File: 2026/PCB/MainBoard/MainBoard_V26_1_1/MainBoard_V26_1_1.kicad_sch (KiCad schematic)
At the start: 0 parts

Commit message: 446追加
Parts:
- added U1: STM32F446RETx, Package_QFP:LQFP-64_10x10mm_P0.5mm, symbol MCU_ST_STM32F4:STM32F446RETx
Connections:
- new net: U1.18 (VSS), U1.31 (VSS), U1.47 (VSS), U1.63 (VSS)
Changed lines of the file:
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@@
 	(generator_version "9.0")
 	(paper "A4")
+	(symbol
+		(lib_id "MCU_ST_STM32F4:STM32F446RETx")
+		(at 101.6 92.71 0)
+		(unit 1)
+		(exclude_from_sim no)
+		(in_bom yes)
+		(on_board yes)
+		(dnp no)
+		(fields_autoplaced yes)
+		(property "Reference" "U1"
+			(at 106.2833 138.43 0)
+			(effects
+				(font
+					(size 1.27 1.27)
+				)
+				(justify left)
+			)
+		)
+		(property "Value" "STM32F446RETx"
+			(at 106.2833 140.97 0)
+			(effects
+				(font
+					(size 1.27 1.27)
+				)
+				(justify left)
+			)
+		)
+		(property "Footprint" "Package_QFP:LQFP-64_10x10mm_P0.5mm"
+			(at 83.82 135.89 0)
+			(effects
+				(font
+					(size 1.27 1.27)
+				)
+				(justify right)
+				(hide yes)
+			)
+		)
+		(property "Datasheet" "https://www.st.com/resource/en/datasheet/stm32f446re.pdf"
+			(at 101.6 92.71 0)
+			(effects
+				(font
+					(size 1.27 1.27)
+				)
+				(hide yes)
+			)
+		)
+		(property "Description" "STMicroelectronics Arm Cortex-M4 MCU, 512KB flash, 128KB RAM, 180 MHz, 1.8-3.6V, 50 GPIO, LQFP64"
+			(at 101.6 92.71 0)
+			(effects
+				(font
+					(size 1.27 1.27)
+				)
+				(hide yes)
+			)
+		)
+		(pin "50"
+		)
+		(pin "55"
+		)
+		(pin "57"
+		)
+		(pin "46"
+		)
+		(pin "49"
+		)
+		(pin "34"
+		)
+		(pin "26"
+		)
+		(pin "27"
+		)
+		(pin "56"
+		)
+		(pin "58"
+		)
+		(pin "28"
+		)
+		(pin "62"
+		)
+		(pin "29"
+		)
+		(pin "33"
+		)
+		(pin "35"
+		)
+		(pin "59"
+		)
+		(pin "36"
+		)
+		(pin "61"
+		)
+		(pin "5"
+		)
+		(pin "25"
+		)
+		(pin "37"
+		)
+		(pin "24"
+		)
+		(pin "39"
+		)
+		(pin "52"
+		)
+		(pin "2"
+		)
+		(pin "4"
+		)
+		(pin "6"
+		)
+		(pin "60"
+		)
+		(pin "54"
+		)
+		(pin "8"
+		)
+		(pin "7"
+		)
+		(pin "9"
+		)
+		(pin "10"
+		)
+		(pin "11"
+		)
+		(pin "38"
+		)
+		(pin "51"
+		)
+		(pin "40"
+		)
+		(pin "53"
+		)
+		(pin "3"
+		)
+		(pin "30"
+		)
+		(pin "1"
+		)
+		(pin "19"
+		)
+		(pin "32"
+		)
+		(pin "48"
+		)
+		(pin "16"
+		)
+		(pin "17"
+		)
+		(pin "43"
+		)
+		(pin "64"
+		)
+		(pin "13"
+		)
+		(pin "14"
+		)
+		(pin "21"
+		)
+		(pin "45"
+		)
+		(pin "23"
+		)
+		(pin "12"
+		)
+		(pin "31"
+		)
+		(pin "42"
+		)
+		(pin "20"
+		)
+		(pin "41"
+		)
+		(pin "63"
+		)
+		(pin "15"
+		)
+		(pin "22"
+		)
+		(pin "44"
+		)
+		(pin "47"
+		)
+		(pin "18"
+		)
+		(instances
+			(project ""
+				(path "/1e41cf15-e032-452e-b093-2e98e4f5d157"
+					(reference "U1")
+					(unit 1)
+				)
+			)
+		)
+	)
 	(sheet_instances
 		(path "/"

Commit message: ライブラリ一部追加、不要部分削除
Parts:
- added ///J10: ADC3, Connector_JST:JST_PH_S3B-PH-K_1x03_P2.00mm_Horizontal, symbol Connector:Conn_01x03_Socket
- added //D1, //D2, D10, D11, D13, D14, D15, D3, D7, D8, D9: LED, LED_SMD:LED_0603_1608Metric_Pad1.05x0.95mm_HandSolder, symbol Device:LED
- added //J4, J16: CAN_CON, Connector_JST:JST_PH_S2B-PH-K_1x02_P2.00mm_Horizontal, symbol Connector:Conn_01x02_Socket
- added //J8: ADC1, Connector_JST:JST_PH_S3B-PH-K_1x03_P2.00mm_Horizontal, symbol Connector:Conn_01x03_Socket
- added //J9: ADC2, Connector_JST:JST_PH_S3B-PH-K_1x03_P2.00mm_Horizontal, symbol Connector:Conn_01x03_Socket
- added //R1, //R2, R11, R12, R13, R14, R15, R16, R17, R18, R19, R6: 1k, Resistor_SMD:R_0603_1608Metric_Pad0.98x0.95mm_HandSolder, symbol Device:R
- added C1, C8: 4.7u, Capacitor_SMD:C_0603_1608Metric_Pad1.08x0.95mm_HandSolder, symbol Device:C
- added C10, C12, C16, C2, C3, C4, C5, C6, C7: 0.1u, Capacitor_SMD:C_0603_1608Metric_Pad1.08x0.95mm_HandSolder, symbol Device:C
- added C24: 1000u, Capacitor_SMD:CP_Elec_8x10.5, symbol Device:C_Polarized
- added C9: 1u, Capacitor_SMD:C_0603_1608Metric_Pad1.08x0.95mm_HandSolder, symbol Device:C
- added D6: 1N4148W, Diode_SMD:D_SOD-123, symbol Diode:1N4148W
- added H1, H2, H4, H5: MountingHole_Pad, MountingHole:MountingHole_3.2mm_M3_Pad_Via, symbol Mechanical:MountingHole_Pad
- added J1: Raspberry_Pi_2_3, MainBoard:raspberreyPi_2_3, symbol Connector:Raspberry_Pi_2_3
- added J11, J12: //ADC2, Connector_JST:JST_PH_S3B-PH-K_1x03_P2.00mm_Horizontal, symbol Connector:Conn_01x03_Socket
- added J13: //Drib, Connector_JST:JST_PH_S2B-PH-K_1x02_P2.00mm_Horizontal, symbol Connector:Conn_01x02_Socket
- added J14: UART, Connector_JST:JST_PH_S4B-PH-K_1x04_P2.00mm_Horizontal, symbol Connector:Conn_01x04_Socket
- added J15: TFT3, Connector_PinHeader_2.54mm:PinHeader_1x04_P2.54mm_Vertical, symbol Connector:Conn_01x04_Socket
- added J2: fan, Resistor_SMD:R_2816_7142Metric_Pad3.20x4.45mm_HandSolder, symbol Connector:Conn_01x02_Pin
- added J4: metor, Resistor_SMD:R_MiniMELF_MMA-0204, symbol Connector:Conn_01x02_Pin
- added J6: Debug, Connector_JST:JST_XH_S7B-XH-A_1x07_P2.50mm_Horizontal, symbol Connector:Conn_01x07_Pin
- added J7: //ADC0, Connector_JST:JST_PH_S3B-PH-K_1x03_P2.00mm_Horizontal, symbol Connector:Conn_01x03_Socket
- added J8: MOLEX MINISPOX, Connector_Molex:Molex_SPOX_5268-05A_1x05_P2.50mm_Horizontal, symbol Connector:Conn_01x05_Socket
- added LS1: PKLCS1212E4001-R1, MainBoard:SPKR_PKLCS1212E4001-R1, symbol MainBoard:PKLCS1212E4001-R1
- added Q1, Q2: Q_NMOS_GSD, Package_TO_SOT_SMD:SOT-23-3, symbol Device:Q_NMOS_GSD
- added R1, R5, R7: 10k, Resistor_SMD:R_0603_1608Metric_Pad0.98x0.95mm_HandSolder, symbol Device:R
- added R10: 4.7k, Resistor_SMD:R_0603_1608Metric_Pad0.98x0.95mm_HandSolder, symbol Device:R
- added R20: 120, Resistor_SMD:R_0603_1608Metric_Pad0.98x0.95mm_HandSolder, symbol Device:R
- added R8, R9: 2.2k, Resistor_SMD:R_0603_1608Metric_Pad0.98x0.95mm_HandSolder, symbol Device:R
- added ROTSW1: SW_Coded_SH-7070, Button_Switch_THT:Nidec_Copal_SH-7010C, symbol Switch:SW_Coded_SH-7070
- added SW1, SW5, SW6: SW_MEC_5E, MainBoard:SW_SKRPACE010, symbol Switch:SW_MEC_5E
- added SW2: Ras_1, Button_Switch_THT:SW_PUSH_6mm_H7.3mm, symbol Switch:SW_Omron_B3FS
- added SW3: Ras_2, Button_Switch_THT:SW_PUSH_6mm_H7.3mm, symbol Switch:SW_Omron_B3FS
- added SW4: SW_Wuerth_450301014042, MainBoard:slideSW, symbol Switch:SW_Wuerth_450301014042
- added U10: MPU9250, Connector_PinHeader_2.54mm:PinHeader_1x10_P2.54mm_Vertical, symbol MainBoard:MPU9250
- added U2: LMR51460FSQDRRRQ1, DRR0012E-IPC_A, symbol 2025-11-16_00-40-10:LMR51460FSQDRRRQ1
- added U3: MOUDLE-SEEEDUINO-XIAO, MainBoard:MOUDLE14P-SMD-2.54-21X17.8MM, symbol MainBoard:MOUDLE-SEEEDUINO-XIAO
- added U4: ~, Connector_PinHeader_2.54mm:PinHeader_1x13_P2.54mm_Vertical, symbol MainBoard:TFT
- added U6: BNO055, Connector_PinHeader_2.54mm:PinHeader_1x04_P2.54mm_Vertical, symbol MainBoard:BNO055
- added U8: MAX3051, Package_SO:SOIC-8_3.9x4.9mm_P1.27mm, symbol Interface_UART:MAX3051
- added Y1: CSTNE16M0V530000R0, MainBoard:OSC_CSTNE16M0V530000R0, symbol MainBoard:CSTNE16M0V530000R0
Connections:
- net +3.3V: now reaches U1.1 (VBAT)
- net +3.3V: now also U1.13 (VDDA), U1.19 (VDD), U1.32 (VDD), U1.48 (VDD), U1.64 (VDD), ///J10.2 (Pin_2), //J8.2 (Pin_2), //J9.2 (Pin_2), C16.1, C2.2, C3.2, C4.2, C5.2, C6.2, C7.2, C8.1, D11.2 (A), J11.2 (Pin_2), J12.2 (Pin_2), J14.1 (Pin_1), J6.6 (Pin_6), J7.2 (Pin_2), R5.1, R8.2, R9.2, SW4.2 (C), U10.1 (VCC), U3.12 (3V3), U4.1 (VCC), U6.1 (5V), U8.3 (VDD)
- net LED3: now reaches U1.10 (PC2)
- net LED3: now also //D1.2 (A)
- net LED4: now reaches U1.11 (PC3)
- net LED4: now also //D2.2 (A)
- net GND: now reaches U1.12 (VSSA)
- net GND: now also U1.18 (VSS), U1.31 (VSS), U1.47 (VSS), U1.63 (VSS), ///J10.3 (Pin_3), //J8.3 (Pin_3), //J9.3 (Pin_3), //R1.2, //R2.2, C1.2, C10.2, C12.2, C16.2, C2.1, C24.2, C3.1, C4.1, C5.1, C6.1, C7.1, C8.2, C9.2, D13.1 (K), D14.1 (K), J1.14 (GND), J1.20 (GND), J1.25 (GND), J1.30 (GND), J1.34 (GND), J1.39 (GND), J1.6 (GND), J1.9 (GND), J11.3 (Pin_3), J12.3 (Pin_3), J13.2 (Pin_2), J14.2 (Pin_2), J15.1 (Pin_1), J15.2 (Pin_2), J15.3 (Pin_3), J15.4 (Pin_4), J2.2 (Pin_2), J4.1 (Pin_1), J6.7 (Pin_7), J7.3 (Pin_3), J8.1 (Pin_1), Q1.2 (S), Q2.2 (S), R1.2, R11.2, R12.2, R13.2, R14.2, R15.2, R16.2, R17.2, R6.2, ROTSW1.C, SW1.1, SW1.2, SW2.1, SW3.1, SW4.3 (A), SW5.1, SW5.2, SW6.1, SW6.2, U10.10 (FSYNC), U10.2 (GND), U3.13 (GND), U4.2 (GND), U6.2 (GND), U8.2 (GND), U8.5 (SHDN), U8.8 (RS), Y1.2
- net BATTERY_MEASURE: now reaches U1.14 (PA0)
- net BATTERY_MEASURE: now also D6.1 (K)
- net ADC_SUB1: now reaches U1.15 (PA1)
- net ADC_SUB1: now also //J8.1 (Pin_1)
- net UART2_TX: now reaches U1.16 (PA2)
- net UART2_TX: now also J14.3 (Pin_3)
- net UART2_RX: now reaches U1.17 (PA3)
- net UART2_RX: now also J14.4 (Pin_4)
- net ADC_SUB0: now reaches U1.20 (PA4)
- net ADC_SUB0: now also J7.1 (Pin_1)
- net LED0: now reaches U1.21 (PA5)
- net LED0: now also D7.2 (A)
- net ADC_PHOTO0: now reaches U1.22 (PA6)
- net ADC_PHOTO0: now also J11.1 (Pin_1)
- net ADC_PHOTO1: now reaches U1.23 (PA7)
- net ADC_PHOTO1: now also J12.1 (Pin_1)
- net ADC_SUB2: now reaches U1.24 (PC4)
- net ADC_SUB2: now also //J9.1 (Pin_1)
- net ADC_SUB3: now reaches U1.25 (PC5)
- net ADC_SUB3: now also ///J10.1 (Pin_1)
- net SPI2.INT: now reaches U1.29 (PB10)
- net SPI2.INT: now also U10.8 (INT)
- net at U1.30 (VCAP_1): now also C1.1
- net SPI2.CS: now reaches U1.33 (PB12)
- net SPI2.CS: now also U10.9 (NCS)
- net SPI2.CLK: now reaches U1.34 (PB13)
- net SPI2.CLK: now also U10.3 (SCL:CLK)
- net SPI2.MISO: now reaches U1.35 (PB14)
- net SPI2.MISO: now also U10.7 (ADO:MISO)
- net SPI2.MOSI: now reaches U1.36 (PB15)
- net SPI2.MOSI: now also U10.4 (SDA:MOSI)
- net discharge: now reaches U1.38 (PC7)
- net discharge: now also SW6.3 (K), SW6.4 (A)
- net imu.reset: now reaches U1.39 (PC8)
- net imu.reset: now also SW5.3 (K), SW5.4 (A)
- net HEART_BEAT_LED: now reaches U1.41 (PA8)
- net HEART_BEAT_LED: now also D10.2 (A)
- net SWDIO: now reaches U1.46 (PA13)
- net SWDIO: now also J6.5 (Pin_5)
- net SWCLK: now reaches U1.49 (PA14)
- net SWCLK: now also J6.4 (Pin_4)
- net at U1.5 (PH0): now also Y1.1
- net UART4_TX: now reaches U1.51 (PC10)
- net UART4_TX: now also U3.4 (PA11_A3_D3)
- net UART4_RX: now reaches U1.52 (PC11)
- net UART4_RX: now also U3.3 (PA10_A2_D2)
- net Ras_RX: now reaches U1.53 (PC12)
- net Ras_RX: now also J1.10 (GPIO15/RXD)
- net Ras_TX: now reaches U1.54 (PD2)
- net Ras_TX: now also J1.8 (GPIO14/TXD)
- net DRIB_OUT: now reaches U1.56 (PB4)
- net DRIB_OUT: now also J13.1 (Pin_1)
- net I2C_SCL: now reaches U1.58 (PB6)
- net I2C_SCL: now also R9.1, U6.4 (SCL)
- net I2C_SDA: now reaches U1.59 (PB7)
- net I2C_SDA: now also R8.1, U6.3 (SDA)
- net at U1.6 (PH1): now also Y1.3
- net at U1.60 (BOOT0): now also R1.1, SW4.1 (B)
- net CAN1_RX: now reaches U1.61 (PB8)
- net CAN1_RX: now also U8.4 (RXD)
- net CAN1_TX: now reaches U1.62 (PB9)
- net CAN1_TX: now also U8.1 (TXD)
- net NRST: now reaches U1.7 (NRST)
- net NRST: now also J6.3 (Pin_3), R5.2, SW1.3 (K), SW1.4 (A)
- net LED1: now reaches U1.8 (PC0)
- net LED1: now also D8.2 (A)
- net LED2: now reaches U1.9 (PC1)
- net LED2: now also D9.2 (A)
- new net: D6.2 (A), R10.2, R11.1
- new net: LS1.N, Q1.3 (D), Q2.3 (D), R7.2
- new net: D9.1 (K), R14.1
- new net: //D1.1 (K), //R1.1
- new net: D15.1 (K), R17.1
- new net: D3.1 (K), R6.1
- new net: D10.1 (K), R15.1
- new net: D8.1 (K), R13.1
- new net: J1.1 (3V3), J1.17 (3V3)
- new net: //D2.1 (K), //R2.1
- new net: D11.1 (K), R16.1
- new net: D14.2 (A), R19.2
- new net: D13.2 (A), R18.2
- new net: D7.1 (K), R12.1
- new net +5V: C10.1, C12.1, C24.1, C9.1, D3.2 (A), J1.2 (5V), J1.4 (5V), J2.1 (Pin_1), U3.14 (5V)
- new net +6V: D15.2 (A), J8.3 (Pin_3)
- new net CANH: //J4.1 (Pin_1), J16.2 (Pin_2), J8.4 (Pin_4), R20.1, U8.7 (CANH)
- new net CANL: //J4.2 (Pin_2), J16.1 (Pin_1), J8.5 (Pin_5), R20.2, U8.6 (CANL)
- new net D/C: U3.2 (PA4_A1_D1), U4.5 (D/C)
- new net LCD_LED: U3.7 (PB08_A6_D6_TX), U4.8 (LED)
- new net LED_CS: U3.8 (PB09_A7_D7_RX), U4.3 (CS)
- new net LED_RAS1: J1.12 (GPIO18/PWM0), R18.1
- new net LED_RAS2: J1.13 (GPIO27), R19.1
- new net MISO: U3.10 (PA5_A9_D9_MISO), U4.13 (T_DOUT)
- new net MOSI: U3.11 (PA6_A10_D10_MOSI), U4.12 (T_DIN), U4.6 (MOSI)
- new net R1: J1.7 (GCLK0/GPIO4), ROTSW1.1
- new net R2: J1.29 (GCLK1/GPIO5), ROTSW1.2
- new net R3: J1.31 (GCLK2/GPIO6), ROTSW1.4
- new net R4: J1.22 (GPIO25), ROTSW1.8
- new net RAS_AUDIO: J1.33 (PWM1/GPIO13), Q1.1 (G)
- new net Reset: U3.1 (PA02_A0_D0), U4.4 (Reset)
- new net SCK: U3.9 (PA7_A8_D8_SCK), U4.10 (T_CLK), U4.7 (SCK)
- new net SW_RAS1: J1.18 (GPIO24), SW2.2
- new net SW_RAS2: J1.15 (GPIO22), SW3.2
- new net T_CS: U3.5 (PA8_A4_D4_SDA), U4.11 (T_CS)
- new net UART1_RX: J6.1 (Pin_1)
- new net UART1_TX: J6.2 (Pin_2)
- new net UI_Audio: Q2.1 (G), U3.6 (PA9_A5_D5_SCL)
- new net VD: J4.2 (Pin_2), J8.2 (Pin_2), LS1.P, R10.1, R7.1
- no-connect marks 0 -> 34
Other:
- note added: "BOOT"
- note added: "Battery Sense"
- note added: "CAN"
- note added: "Connectors"
- note added: "IMU"
- note added: "LEDs"
- note added: "Oscillator"
- note added: "PIEZO"
- note added: "Rasberry Pi"
- note added: "Reset"
- note added: "STLink"
- note added: "STM32F446RE"
- note added: "UI"

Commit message: 電源周りほぼ完成
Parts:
- added C11: 4.7u, symbol Device:C
- added C13, C15: 100n, symbol Device:C
- added C14: 47u, symbol Device:C
- added C? (x2): 10u, Capacitor_SMD:C_0805_2012Metric_Pad1.18x1.45mm_HandSolder, symbol Device:C
- added L1: 4.7u, symbol Device:L
- added R2: 27k, symbol Device:R
- added R21, R3: 100k, symbol Device:R
- added R4: 19.1k, symbol Device:R
- added U5: MCP1703AT-3302E/CB, Package_TO_SOT_SMD:TSOT-23, symbol WheelVoltageBooster_LIB_SYM:MCP1703AT-3302E/CB
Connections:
- net +5V is gone; now on net +24V: C10.1, C12.1, C24.1, C9.1, D3.2 (A), J1.2 (5V), J1.4 (5V), J2.1 (Pin_1), U3.14 (5V)
- net GND: now also C?.2, C?.2, U5.1 (GND)
- net at U2.1 (SW): now also U2.2 (SW), U2.3 (SW), C15.2, L1.1
- net +24V: now reaches U2.10 (VIN)
- net +24V: now also U2.11 (VIN), U2.12 (VIN), U2.13 (PGND_DAP), U2.8 (AGND), U2.9 (EN), C11.1, C11.2, C13.1, C13.2, C14.1, C14.2, C?.1, L1.2, R2.2, R21.2, R3.1, R4.2, U5.3 (Vin)
- net at U2.4 (BOOT): now also C15.1
- net at U2.5 (PG): now also R3.2
- net at U2.6 (RT): now also R2.1
- net at U2.7 (FB): now also R21.1, R4.1
- new net +3V3: C?.1, U5.2 (Vout)
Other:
- moved on the sheet: U2

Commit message: 通信回りたぶん完成
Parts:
- removed ///J10: ADC3, Connector_JST:JST_PH_S3B-PH-K_1x03_P2.00mm_Horizontal, symbol Connector:Conn_01x03_Socket
- removed //J8: ADC1, Connector_JST:JST_PH_S3B-PH-K_1x03_P2.00mm_Horizontal, symbol Connector:Conn_01x03_Socket
- removed //J9: ADC2, Connector_JST:JST_PH_S3B-PH-K_1x03_P2.00mm_Horizontal, symbol Connector:Conn_01x03_Socket
- removed J11, J12: //ADC2, Connector_JST:JST_PH_S3B-PH-K_1x03_P2.00mm_Horizontal, symbol Connector:Conn_01x03_Socket
- removed J14: UART, Connector_JST:JST_PH_S4B-PH-K_1x04_P2.00mm_Horizontal, symbol Connector:Conn_01x04_Socket
- removed J7: //ADC0, Connector_JST:JST_PH_S3B-PH-K_1x03_P2.00mm_Horizontal, symbol Connector:Conn_01x03_Socket
- U2: footprint DRR0012E-IPC_A -> 0_Library:DRR0012E-IPC_A
- gave numbers to parts that had none: 2
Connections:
- net +3V3 is gone; now on net +3.3V: C17.1, U5.2 (Vout)
- net ADC_SUB1 is gone; now on net UART4_RX: U1.15 (PA1)
- net BATTERY_MEASURE: no longer U1.14 (PA0)
- net LED0: no longer U1.21 (PA5)
- net LED1: no longer U1.8 (PC0)
- net LED2: no longer U1.9 (PC1)
- net LED3: no longer U1.10 (PC2)
- net LED4: no longer U1.11 (PC3)
- net UART1_RX: now also U1.43 (PA10)
- net UART1_TX: now also U1.42 (PA9)
- net UART4_RX: no longer U1.52 (PC11)
- net UART4_TX: now also U1.14 (PA0); no longer U1.51 (PC10)
- net discharge: no longer U1.38 (PC7)
- net MD4_RX: now reaches U1.37 (PC6)
- net ADC_PHOTO0: no longer names the net of U1.22 (PA6)
- net ADC_PHOTO1: no longer names the net of U1.23 (PA7)
- net ADC_SUB0: no longer names the net of U1.20 (PA4)
- net ADC_SUB2: no longer names the net of U1.24 (PC4)
- net ADC_SUB3 renamed MD2_TX
- net Ras_RX: no longer names the net of J1.10 (GPIO15/RXD)
- net Ras_RX: no longer U1.53 (PC12)
- net Ras_TX: no longer names the net of J1.8 (GPIO14/TXD)
- net Ras_TX: no longer U1.54 (PD2)
- net UART2_RX renamed MD1_TX
- net UART2_TX renamed MD1_RX
- new net MD2_RX: U1.51 (PC10)
- new net MD3_RX: U1.53 (PC12)
- new net MD3_TX: U1.54 (PD2)
- new net MD4_TX: U1.38 (PC7)
- no-connect marks 34 -> 33

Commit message: 通信回りたぶん完成2
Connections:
- net CAN1_RX: now also U1.44 (PA11); no longer U1.61 (PB8)
- net CAN1_TX: now also U1.45 (PA12); no longer U1.62 (PB9)
- net SPI2.CLK: now also J1.23 (SCLK0/GPIO11), U1.29 (PB10); no longer U1.34 (PB13), U10.3 (SCL:CLK)
- net SPI2.CS: now also J1.32 (PWM0/GPIO12), U1.28 (PB2); no longer U1.33 (PB12), U10.9 (NCS)
- net SPI2.MISO: now also J1.21 (MISO0/GPIO9), U1.10 (PC2); no longer U1.35 (PB14), U10.7 (ADO:MISO)
- net SPI2.MOSI: now also J1.19 (MOSI0/GPIO10), U1.9 (PC1); no longer U1.36 (PB15), U10.4 (SDA:MOSI)
- net SPI1.CLK: now reaches U1.21 (PA5)
- net SPI1.CLK: now also U10.3 (SCL:CLK)
- net SPI1.MISO: now reaches U1.22 (PA6)
- net SPI1.MISO: now also U10.7 (ADO:MISO)
- net SPI1.MOSI: now reaches U1.23 (PA7)
- net SPI1.MOSI: now also U10.4 (SDA:MOSI)
- net SPI1.CS: now reaches U1.24 (PC4)
- net SPI1.CS: now also U10.9 (NCS)
- net SPI2.INT: no longer names the net of U10.8 (INT)
- net SPI2.INT: no longer U1.29 (PB10)
- no-connect marks 33 -> 27

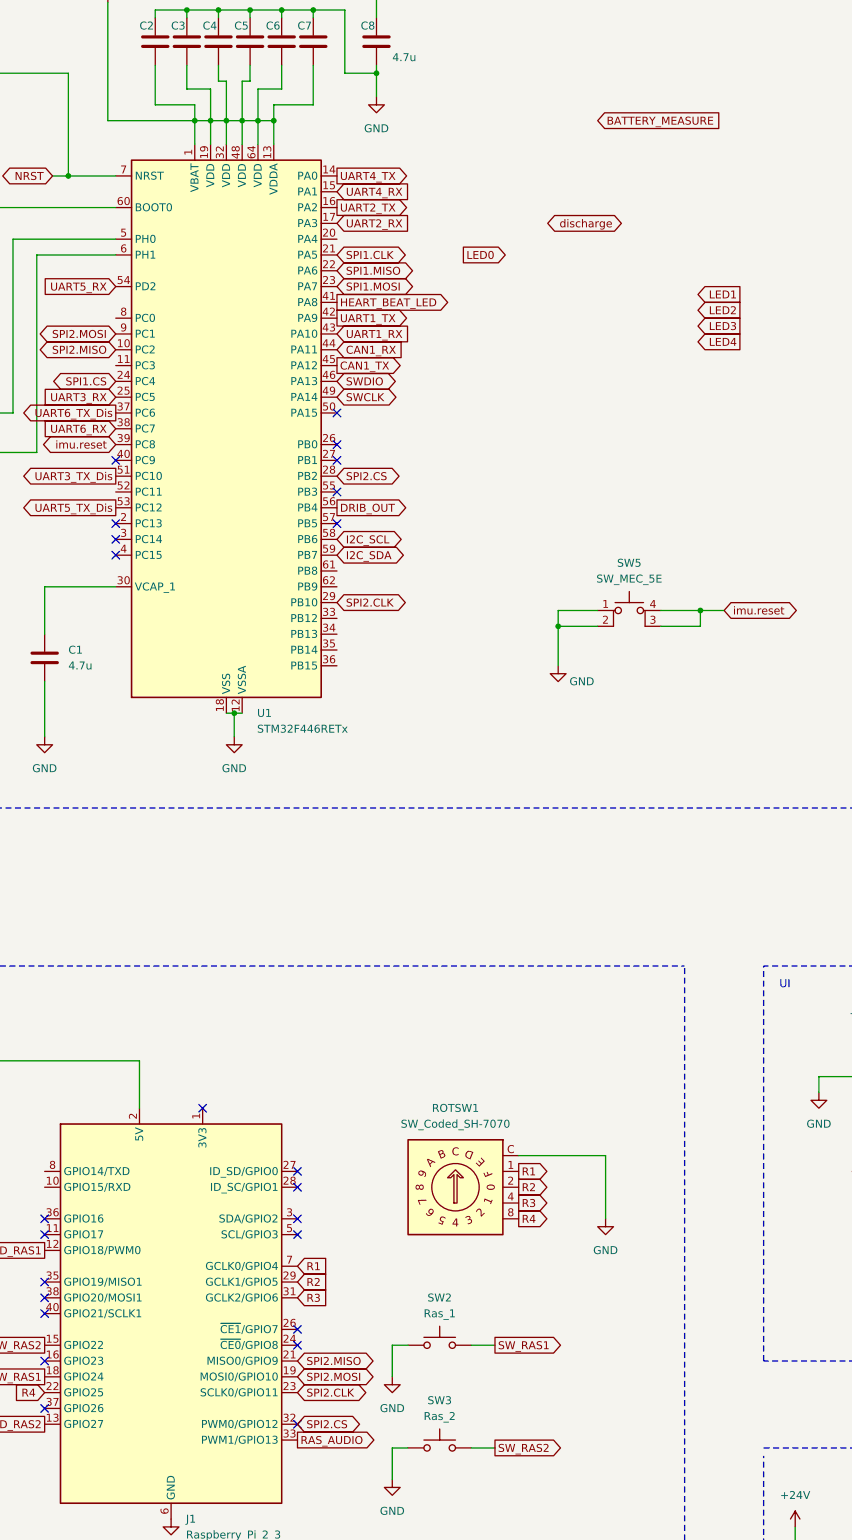
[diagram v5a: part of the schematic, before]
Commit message: 一部フットプリント割り当て以外回路完成、PCB配線開始
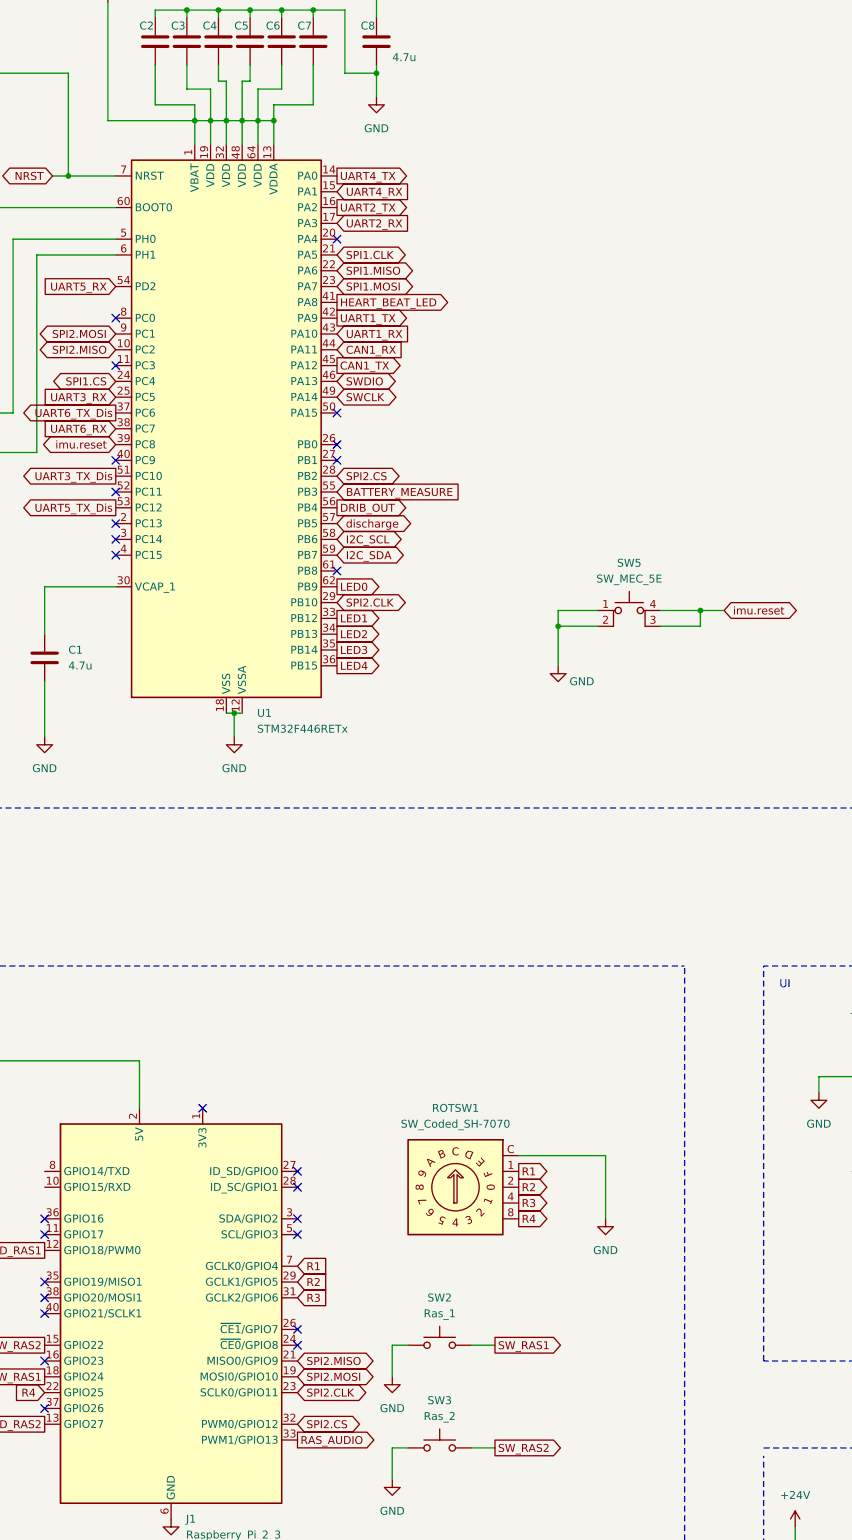
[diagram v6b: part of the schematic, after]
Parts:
- C11, C13, C15: footprint (none) -> Capacitor_SMD:C_0603_1608Metric_Pad1.08x0.95mm_HandSolder
- J1: footprint MainBoard:raspberreyPi_2_3 -> 0_Library:raspberreyPi_2_3
- LS1: footprint MainBoard:SPKR_PKLCS1212E4001-R1 -> 0_Library:SPKR_PKLCS1212E4001-R1
- SW1, SW5, SW6: footprint MainBoard:SW_SKRPACE010 -> 0_Library:SW_SKRPACE010
- SW4: footprint MainBoard:slideSW -> 0_Library:slideSW
- U3: footprint MainBoard:MOUDLE14P-SMD-2.54-21X17.8MM -> 0_Library:MOUDLE14P-SMD-2.54-21X17.8MM
- Y1: footprint MainBoard:OSC_CSTNE16M0V530000R0 -> 0_Library:OSC_CSTNE16M0V530000R0
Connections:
- net BATTERY_MEASURE: now also U1.55 (PB3)
- net LED0: now also U1.62 (PB9)
- net LED1: now also U1.33 (PB12)
- net LED2: now also U1.34 (PB13)
- net LED3: now also U1.35 (PB14)
- net LED4: now also U1.36 (PB15)
- net discharge: now also U1.57 (PB5)
- no-connect marks 27 -> 29
